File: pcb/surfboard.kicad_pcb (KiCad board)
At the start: 2 copper layers, 64.3 x 45.2 mm, 24 parts, among them SW1 SW_PUSH, SW2 SW_PUSH, SW3 SW_PUSH, SW4 SW_PUSH, SW5 SW_PUSH, SW6 SW_PUSH, SW7 SW_PUSH, U1 ProMicro

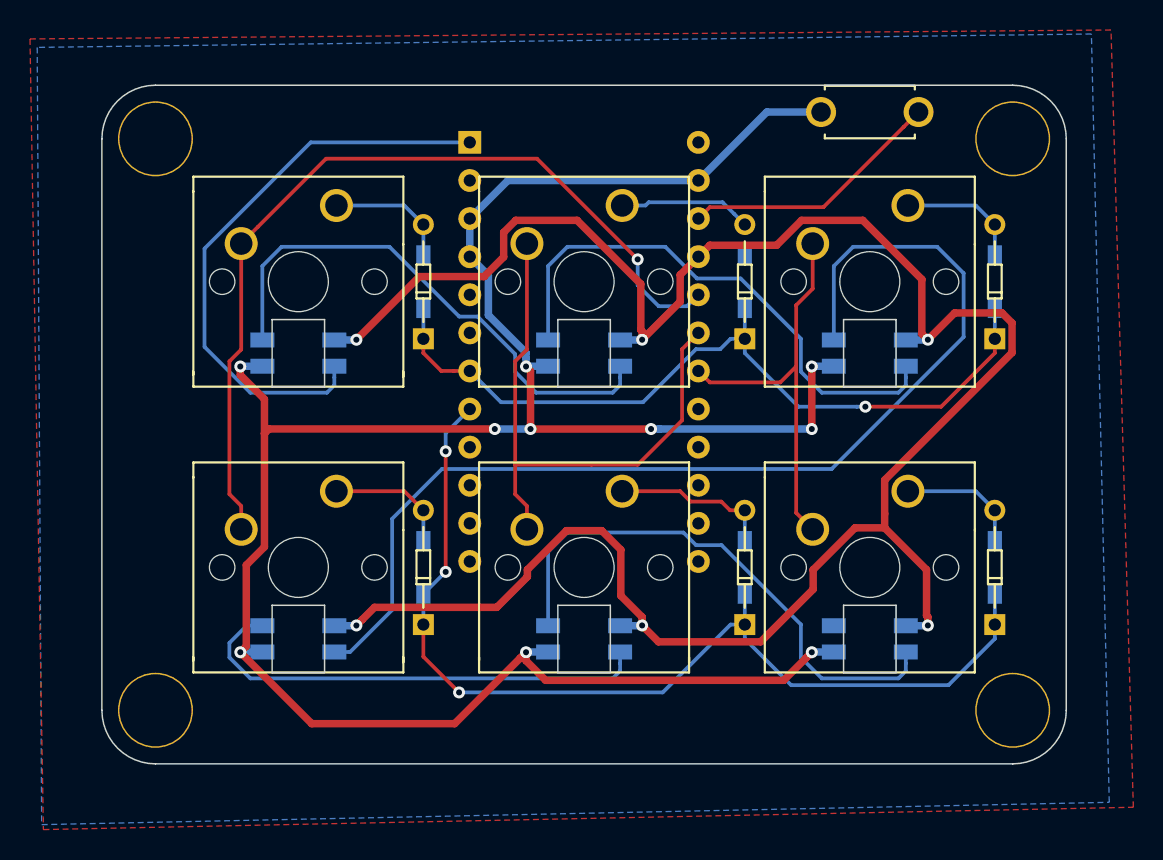
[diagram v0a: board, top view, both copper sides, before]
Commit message: Adjust LED hole positions
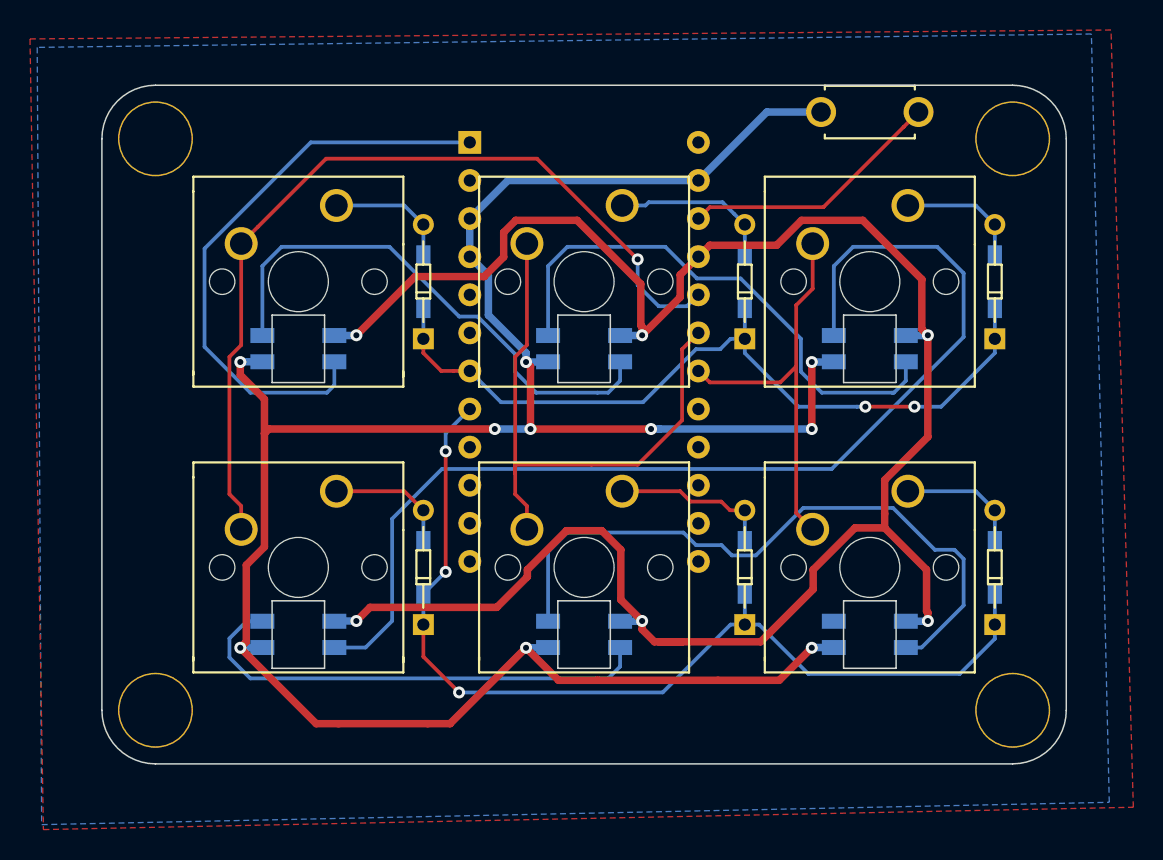
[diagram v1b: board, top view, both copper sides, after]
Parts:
- moved L1 0.30 mm to (72.4, 61.8)
- moved L2 0.30 mm to (72.4, 80.9)
- moved L3 0.30 mm to (91.4, 61.8)
- moved L4 0.30 mm to (91.4, 80.9)
- moved L5 0.30 mm to (110.5, 61.8)
- moved L6 0.30 mm to (110.5, 80.9)
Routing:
- net VCC: track 145.1 -> 135.7 mm
- net Net-(L4-Pad1): track 36.1 -> 44.3 mm
- net Net-(D3-Pad2): track 8.88 -> 10.9 mm
- net row1: track 67.3 -> 66.1 mm
- net col1: track 38.3 -> 38.9 mm
- net row0: vias 1 -> 2
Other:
- outline, holes or cut-outs redrawn

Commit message: Store ResetSW backside and move screws
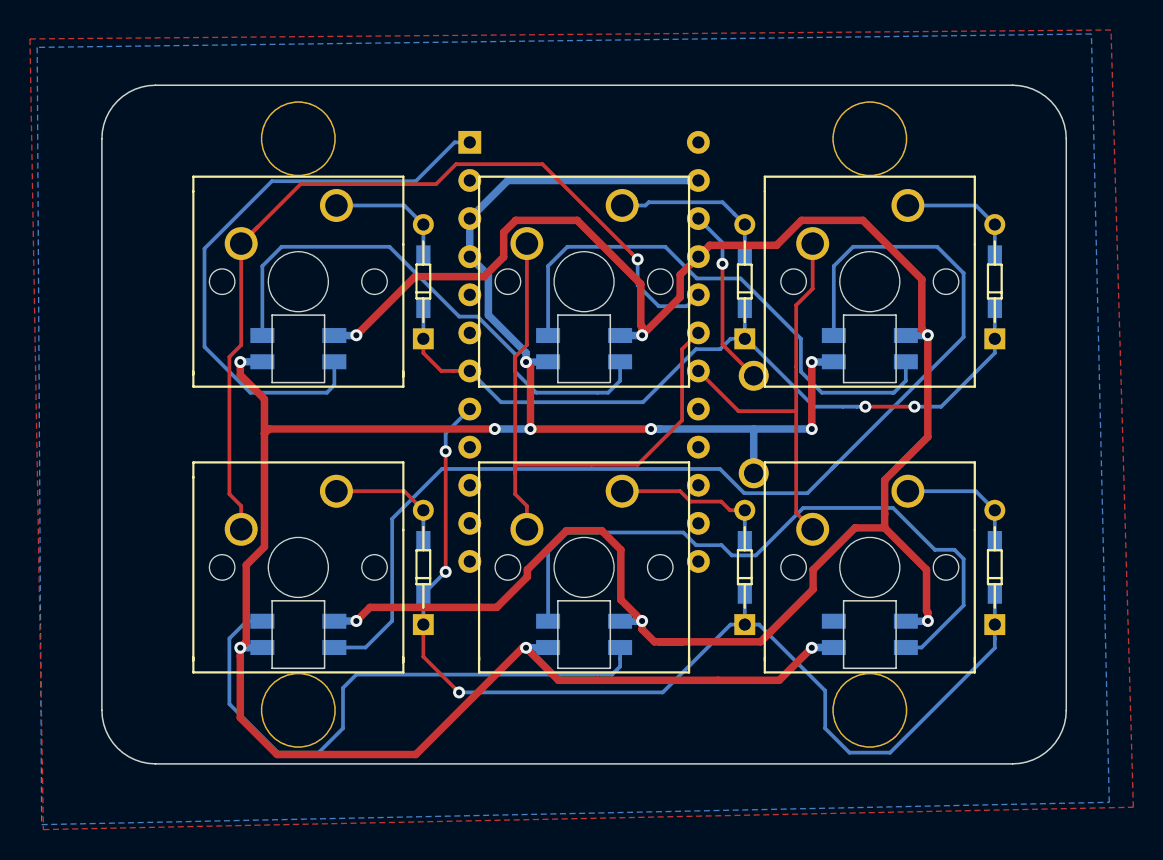
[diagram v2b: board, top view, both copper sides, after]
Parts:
- SW1: moved to B.Cu
- moved SW1 22.2 mm to (102.7, 66.9), turned to 270 degrees
- moved Ref** 9.53 mm to (72.4, 86.0)
- moved Ref** 9.53 mm to (110.5, 47.9)
- moved Ref** 9.53 mm to (110.5, 86.0)
- moved Ref** 9.53 mm to (72.4, 47.9)
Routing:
- net Net-(L2-Pad1): track 32.2 -> 39.7 mm
- net row1: track 66.1 -> 72.3 mm
- net reset: track 17.6 -> 12.0 mm, vias 0 -> 1
- net GND: track 156.4 -> 153.8 mm
- net Net-(L2-Pad3): track 73.3 -> 75.3 mm
- net col0: track 57.9 -> 59.2 mm
- net row0: track 53.2 -> 52.6 mm
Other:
- board text added: "hifumi keyboard v0.1 by riconken"
- board text removed: "hifumi keyboard 0.1 produced by riconken"
